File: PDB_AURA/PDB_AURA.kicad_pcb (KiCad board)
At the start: 4 copper layers, 50 x 50 mm, 55 parts, among them J100 XT30PW-M, J200 532617010, J201 XT30PW-F, J202 XT30PW-F, J203 XT30PW-F, J204 XT30PW-F, Q200 HSK10N06, Q201 HSK10N06, U101 SI4825DDY-T1-GE3, U2 TPS56C230RJER, U200 LTV-217-B-G, U201 LTV-217-B-G, U202 INA219AIDCNR

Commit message: Initial draft
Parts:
- TP102, TP105: moved to B.Cu
- moved TP105 46.7 mm to (68.0, 73.5), turned to 180 degrees
- moved TP101 36.6 mm to (75.0, 73.0)
- moved TP102 34.1 mm to (77.5, 76.0), turned to 180 degrees
- moved TP104 31.3 mm to (86.5, 80.5)
- moved TP103 30.6 mm to (81.0, 73.0)
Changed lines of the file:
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@@
 	(footprint "TestPoint:TestPoint_Pad_D1.0mm"
 		(layer "F.Cu")
-		(at 114.5 66.45)
+		(at 86.5 80.5)
 		(descr "SMD pad as test Point, diameter 1.0mm")
 		(tags "test point SMD pad")
@@
 	(footprint "TestPoint:TestPoint_Pad_D1.0mm"
 		(layer "F.Cu")
-		(at 111.45 69.5)
+		(at 75 73)
 		(descr "SMD pad as test Point, diameter 1.0mm")
 		(tags "test point SMD pad")
@@
 		)
 	)
-	(footprint "TestPoint:TestPoint_Pad_D1.0mm"
-		(layer "F.Cu")
-		(at 111.45 72.55)
-		(descr "SMD pad as test Point, diameter 1.0mm")
-		(tags "test point SMD pad")
-		(property "Reference" "TP102"
-			(at 0 -1.448 0)
-			(layer "F.SilkS")
-			(hide yes)
-			(effects
-				(font
-					(size 1 1)
-					(thickness 0.15)
-				)
-			)
-		)
-		(property "Value" "TestPoint"
-			(at 0 1.55 0)
-			(layer "F.Fab")
-			(effects
-				(font
-					(size 1 1)
-					(thickness 0.15)
-				)
-			)
-		)
-		(property "Datasheet" ""
-			(at 0 0 0)
-			(unlocked yes)
-			(layer "F.Fab")
-			(hide yes)
-			(effects
-				(font
-					(size 1.27 1.27)
-					(thickness 0.15)
-				)
-			)
-		)
-		(property "Description" "test point"
-			(at 0 0 0)
-			(unlocked yes)
-			(layer "F.Fab")
-			(hide yes)
-			(effects
-				(font
-					(size 1.27 1.27)
-					(thickness 0.15)
-				)
-			)
-		)
-		(property ki_fp_filters "Pin* Test*")
-		(sheetname "/100_Power/")
-		(sheetfile "Power.kicad_sch")
-		(attr exclude_from_pos_files)
-		(fp_circle
-			(center 0 0)
-			(end 0 0.7)
-			(stroke
-				(width 0.12)
-				(type solid)
-			)
-			(fill no)
-			(layer "F.SilkS")
-		)
-		(fp_circle
-			(center 0 0)
-			(end 1 0)
-			(stroke
-				(width 0.05)
-				(type solid)
-			)
-			(fill no)
-			(layer "F.CrtYd")
-		)
-		(fp_text user "${REFERENCE}"
-			(at 0 -1.45 0)
-			(layer "F.Fab")
-			(effects
-				(font
-					(size 1 1)
-					(thickness 0.15)
-				)
-			)
-		)
-		(pad "1" smd circle
-			(at 0 0)
-			(size 1 1)
-			(layers "F.Cu" "F.Mask")
-			(net 49 "/100_Power/FB_5V")
-			(pinfunction "1")
-			(pintype "passive")
-		)
-		(embedded_fonts no)
-	)
 	(footprint "Resistor_SMD:R_0402_1005Metric"
 		(layer "F.Cu")
@@
 	(footprint "TestPoint:TestPoint_Pad_D1.0mm"
 		(layer "F.Cu")
-		(at 111.45 75.6)
+		(at 81 73)
 		(descr "SMD pad as test Point, diameter 1.0mm")
 		(tags "test point SMD pad")
@@
 		(embedded_fonts no)
 	)
-	(footprint "TestPoint:TestPoint_Pad_D1.0mm"
-		(layer "F.Cu")
-		(at 114.5 69.5)
-		(descr "SMD pad as test Point, diameter 1.0mm")
-		(tags "test point SMD pad")
-		(property "Reference" "TP105"
-			(at 0 -1.448 0)
-			(layer "F.SilkS")
-			(hide yes)
-			(effects
-				(font
-					(size 1 1)
-					(thickness 0.15)
-				)
-			)
-		)
-		(property "Value" "TestPoint"
-			(at 0 1.55 0)
-			(layer "F.Fab")
-			(effects
-				(font
-					(size 1 1)
-					(thickness 0.15)
-				)
-			)
-		)
-		(property "Datasheet" ""
-			(at 0 0 0)
-			(unlocked yes)
-			(layer "F.Fab")
-			(hide yes)
-			(effects
-				(font
-					(size 1.27 1.27)
-					(thickness 0.15)
-				)
-			)
-		)
-		(property "Description" "test point"
-			(at 0 0 0)
-			(unlocked yes)
-			(layer "F.Fab")
-			(hide yes)
-			(effects
-				(font
-					(size 1.27 1.27)
-					(thickness 0.15)
-				)
-			)
-		)
-		(property ki_fp_filters "Pin* Test*")
-		(sheetname "/100_Power/")
-		(sheetfile "Power.kicad_sch")
-		(attr exclude_from_pos_files)
-		(fp_circle
-			(center 0 0)
-			(end 0 0.7)
-			(stroke
-				(width 0.12)
-				(type solid)
-			)
-			(fill no)
-			(layer "F.SilkS")
-		)
-		(fp_circle
-			(center 0 0)
-			(end 1 0)
-			(stroke
-				(width 0.05)
-				(type solid)
-			)
-			(fill no)
-			(layer "F.CrtYd")
-		)
-		(fp_text user "${REFERENCE}"
-			(at 0 -1.45 0)
-			(layer "F.Fab")
-			(effects
-				(font
-					(size 1 1)
-					(thickness 0.15)
-				)
-			)
-		)
-		(pad "1" smd circle
-			(at 0 0)
-			(size 1 1)
-			(layers "F.Cu" "F.Mask")
-			(net 7 "/100_Power/rvrs_plr")
-			(pinfunction "1")
-			(pintype "passive")
-		)
-		(embedded_fonts no)
-	)
 	(footprint "Resistor_SMD:R_0402_1005Metric"
 		(layer "F.Cu")
@@
 		)
 	)
+	(footprint "TestPoint:TestPoint_Pad_D1.0mm"
+		(layer "B.Cu")
+		(at 77.5 76 180)
+		(descr "SMD pad as test Point, diameter 1.0mm")
+		(tags "test point SMD pad")
+		(property "Reference" "TP102"
+			(at 0 1.448 0)
+			(layer "B.SilkS")
+			(hide yes)
+			(effects
+				(font
+					(size 1 1)
+					(thickness 0.15)
+				)
+				(justify mirror)
+			)
+		)
+		(property "Value" "TestPoint"
+			(at 0 -1.55 0)
+			(layer "B.Fab")
+			(effects
+				(font
+					(size 1 1)
+					(thickness 0.15)
+				)
+				(justify mirror)
+			)
+		)
+		(property "Datasheet" ""
+			(at 0 0 0)
+			(unlocked yes)
+			(layer "B.Fab")
+			(hide yes)
+			(effects
+				(font
+					(size 1.27 1.27)
+					(thickness 0.15)
+				)
+				(justify mirror)
+			)
+		)
+		(property "Description" "test point"
+			(at 0 0 0)
+			(unlocked yes)
+			(layer "B.Fab")
+			(hide yes)
+			(effects
+				(font
+					(size 1.27 1.27)
+					(thickness 0.15)
+				)
+				(justify mirror)
+			)
+		)
+		(property ki_fp_filters "Pin* Test*")
+		(sheetname "/100_Power/")
+		(sheetfile "Power.kicad_sch")
+		(attr exclude_from_pos_files)
+		(fp_circle
+			(center 0 0)
+			(end 0 -0.7)
+			(stroke
+				(width 0.12)
+				(type solid)
+			)
+			(fill no)
+			(layer "B.SilkS")
+		)
+		(fp_circle
+			(center 0 0)
+			(end 1 0)
+			(stroke
+				(width 0.05)
+				(type solid)
+			)
+			(fill no)
+			(layer "B.CrtYd")
+		)
+		(fp_text user "${REFERENCE}"
+			(at 0 1.45 0)
+			(layer "B.Fab")
+			(effects
+				(font
+					(size 1 1)
+					(thickness 0.15)
+				)
+				(justify mirror)
+			)
+		)
+		(pad "1" smd circle
+			(at 0 0 180)
+			(size 1 1)
+			(layers "B.Cu" "B.Mask")
+			(net 49 "/100_Power/FB_5V")
+			(pinfunction "1")
+			(pintype "passive")
+		)
+		(embedded_fonts no)
+	)
+	(footprint "TestPoint:TestPoint_Pad_D1.0mm"
+		(layer "B.Cu")
+		(at 68 73.5 180)
+		(descr "SMD pad as test Point, diameter 1.0mm")
+		(tags "test point SMD pad")
+		(property "Reference" "TP105"
+			(at 0 1.448 0)
+			(layer "B.SilkS")
+			(hide yes)
+			(effects
+				(font
+					(size 1 1)
+					(thickness 0.15)
+				)
+				(justify mirror)
+			)
+		)
+		(property "Value" "TestPoint"
+			(at 0 -1.55 0)
+			(layer "B.Fab")
+			(effects
+				(font
+					(size 1 1)
+					(thickness 0.15)
+				)
+				(justify mirror)
+			)
+		)
+		(property "Datasheet" ""
+			(at 0 0 0)
+			(unlocked yes)
+			(layer "B.Fab")
+			(hide yes)
+			(effects
+				(font
+					(size 1.27 1.27)
+					(thickness 0.15)
+				)
+				(justify mirror)
+			)
+		)
+		(property "Description" "test point"
+			(at 0 0 0)
+			(unlocked yes)
+			(layer "B.Fab")
+			(hide yes)
+			(effects
+				(font
+					(size 1.27 1.27)
+					(thickness 0.15)
+				)
+				(justify mirror)
+			)
+		)
+		(property ki_fp_filters "Pin* Test*")
+		(sheetname "/100_Power/")
+		(sheetfile "Power.kicad_sch")
+		(attr exclude_from_pos_files)
+		(fp_circle
+			(center 0 0)
+			(end 0 -0.7)
+			(stroke
+				(width 0.12)
+				(type solid)
+			)
+			(fill no)
+			(layer "B.SilkS")
+		)
+		(fp_circle
+			(center 0 0)
+			(end 1 0)
+			(stroke
+				(width 0.05)
+				(type solid)
+			)
+			(fill no)
+			(layer "B.CrtYd")
+		)
+		(fp_text user "${REFERENCE}"
+			(at 0 1.45 0)
+			(layer "B.Fab")
+			(effects
+				(font
+					(size 1 1)
+					(thickness 0.15)
+				)
+				(justify mirror)
+			)
+		)
+		(pad "1" smd circle
+			(at 0 0 180)
+			(size 1 1)
+			(layers "B.Cu" "B.Mask")
+			(net 7 "/100_Power/rvrs_plr")
+			(pinfunction "1")
+			(pintype "passive")
+		)
+		(embedded_fonts no)
+	)
 	(gr_arc

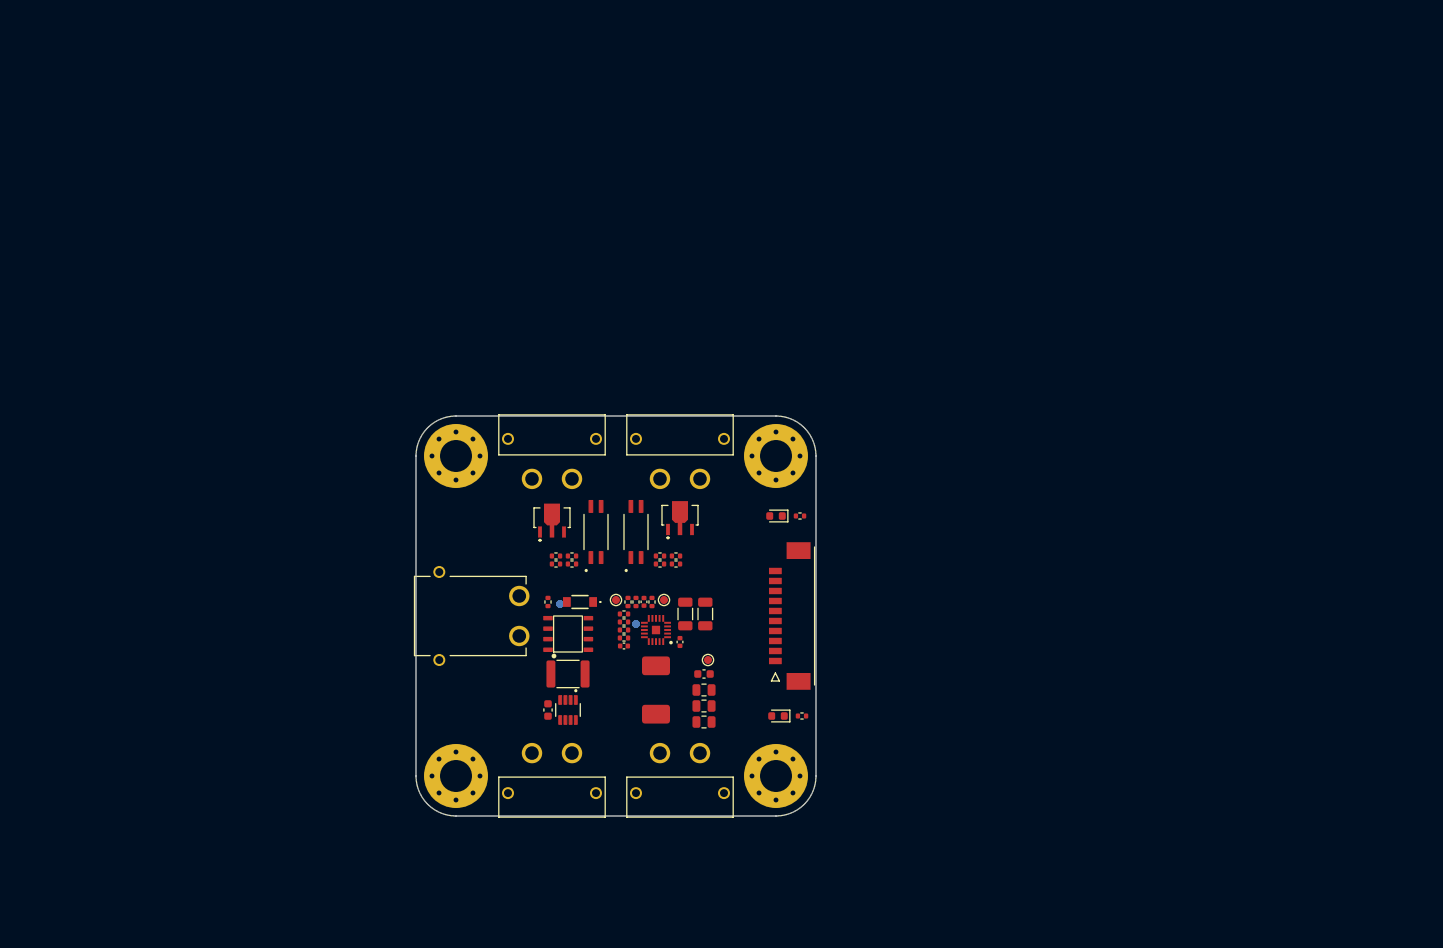
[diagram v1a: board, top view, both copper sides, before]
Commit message: New PDB specs chosen
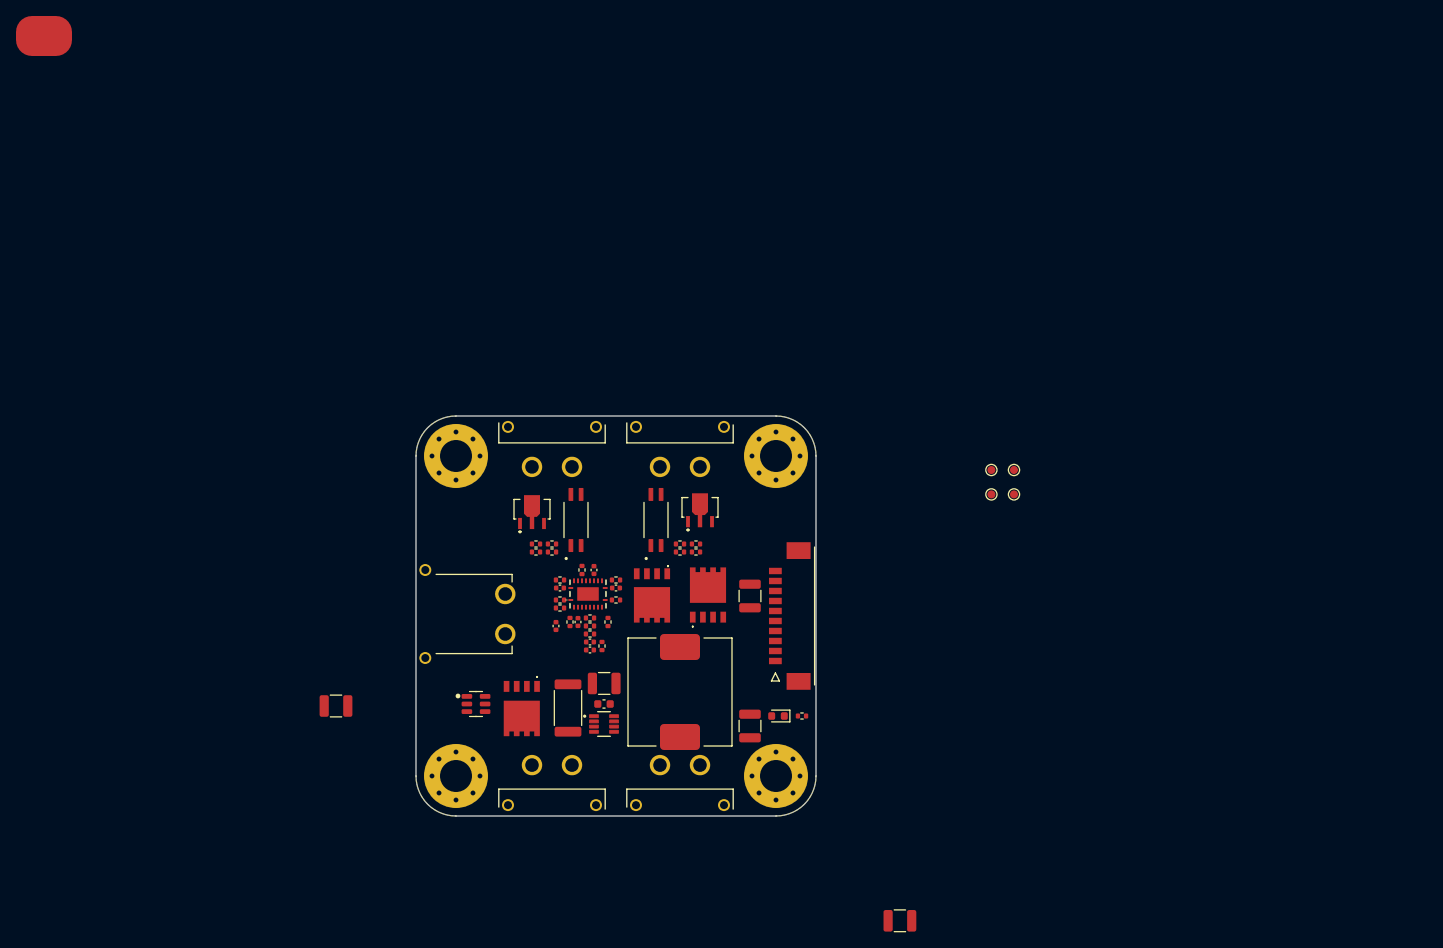
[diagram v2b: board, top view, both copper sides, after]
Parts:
- removed C100: 1u, Capacitor_SMD:C_0402_1005Metric
- removed C101, C102: 22u, Capacitor_SMD:C_1206_3216Metric
- removed C103: 18n, Capacitor_SMD:C_0402_1005Metric
- removed C104: 100n, Capacitor_SMD:C_0402_1005Metric
- removed C105: 100n, Capacitor_SMD:C_0603_1608Metric
- removed C106, C107, C108: 22u, Capacitor_SMD:C_0805_2012Metric
- removed D1: MMSZ5242B, MMSZ5252B:MMSZ5252B
- removed D100: LED, LED_SMD:LED_0603_1608Metric
- removed L100: 1u8, CKST0603:CKST0603-1.5uHM
- removed R102: 49k, Resistor_SMD:R_0402_1005Metric
- removed R103: 13k, Resistor_SMD:R_0402_1005Metric
- removed R104: 180k, Resistor_SMD:R_0402_1005Metric
- removed R105: 33k, Resistor_SMD:R_0402_1005Metric
- removed R106: 330k, Resistor_SMD:R_0402_1005Metric
- removed R107: 110k, Resistor_SMD:R_0402_1005Metric
- removed R108: 15k, Resistor_SMD:R_0402_1005Metric
- removed R109: 680R, Resistor_SMD:R_0402_1005Metric
- removed R110: 100k, Resistor_SMD:R_0402_1005Metric
- removed R111: 0m5, Resistor_SMD:R_1812_4532Metric
- removed TP101, TP102, TP103, TP104, TP105: TestPoint, TestPoint:TestPoint_Pad_D1.0mm
- removed U101: SI4825DDY-T1-GE3, SI4825DDY-T1-GE3:SI4825DDY-T1-GE3
- added C1: 1n, Capacitor_SMD:C_0402_1005Metric, F.Cu at (71.8, 79.2)
- added C10: 47u, Capacitor_SMD:C_1210_3225Metric, F.Cu at (91.8, 72.5)
- added C11: 47u, Capacitor_SMD:C_1210_3225Metric, F.Cu at (73.5, 83.4)
- added C12: 22u, Capacitor_SMD:C_1210_3225Metric, F.Cu at (40.0, 86.2)
- added C13: 22u, Capacitor_SMD:C_1210_3225Metric, F.Cu at (110.5, 113.1)
- added C2: 8n2, Capacitor_SMD:C_0402_1005Metric, F.Cu at (67.5, 76.2)
- added C3: 100n, Capacitor_SMD:C_0402_1005Metric, F.Cu at (70.2, 75.8)
- added C4: 390p, Capacitor_SMD:C_0402_1005Metric, F.Cu at (71.8, 78.2)
- added C5: 100n, Resistor_SMD:R_0402_1005Metric, F.Cu at (70.8, 69.2)
- added C6: 2u2, Capacitor_SMD:C_0402_1005Metric, F.Cu at (72.2, 69.2)
- added C7: 10p, Capacitor_SMD:C_0402_1005Metric, F.Cu at (75.0, 71.5)
- added C8: 100n, Capacitor_SMD:C_0402_1005Metric, F.Cu at (68.0, 71.5)
- added C9: 47u, Capacitor_SMD:C_1210_3225Metric, F.Cu at (91.8, 88.8)
- added J1: ~, SOLDER_PAD:PWR_SOLDER_PAD, F.Cu at (3.50, 2.50)
- added L1: 1u8, 125CDMCCDS-1R8MC:Untitled, F.Cu at (83.0, 84.5)
- added Q1: CSD18540Q5B, CSD18540Q5B:CSD18540Q5B, F.Cu at (86.5, 72.4)
- added Q2: CSD18510Q5B, CSD18510Q5B:CSD18540Q5BT, F.Cu at (79.5, 72.6)
- added Q3: CSD18540Q5B, CSD18540Q5B:CSD18540Q5B, F.Cu at (63.2, 86.6)
- added R1: 18k, Resistor_SMD:R_0402_1005Metric, F.Cu at (71.8, 76.2)
- added R10: 9k1, Resistor_SMD:R_0402_1005Metric, F.Cu at (68.0, 74.0)
- added R11: 2R1, Resistor_SMD:R_0402_1005Metric, F.Cu at (68.0, 70.5)
- added R12: 0m5, Resistor_SMD:R_2512_6332Metric, F.Cu at (69.0, 86.5)
- added R2: 3k4, Resistor_SMD:R_0402_1005Metric, F.Cu at (71.8, 75.2)
- added R3: 1k47, Resistor_SMD:R_0402_1005Metric, F.Cu at (71.8, 77.2)
- added R4: 4k7, Resistor_SMD:R_0402_1005Metric, F.Cu at (69.2, 75.8)
- added R5: 249R, Resistor_SMD:R_0402_1005Metric, F.Cu at (73.2, 78.8)
- added R6: 20k, Resistor_SMD:R_0402_1005Metric, F.Cu at (74.0, 75.8)
- added R7: 576R, Resistor_SMD:R_0402_1005Metric, F.Cu at (75.0, 70.5)
- added R8: 4k7, Resistor_SMD:R_0402_1005Metric, F.Cu at (75.0, 73.0)
- added R9: 35k7, Resistor_SMD:R_0402_1005Metric, F.Cu at (68.0, 73.0)
- added TP1: TestPoint, TestPoint:TestPoint_Pad_D1.0mm, F.Cu at (124.8, 56.8)
- added TP2: TestPoint, TestPoint:TestPoint_Pad_D1.0mm, F.Cu at (124.8, 59.8)
- added TP3: TestPoint, TestPoint:TestPoint_Pad_D1.0mm, F.Cu at (121.9, 56.8)
- added TP4: TestPoint, TestPoint:TestPoint_Pad_D1.0mm, F.Cu at (121.9, 59.8)
- added U1: LM25145RGYR, LM24145RGYR:RGY0020B, F.Cu at (71.5, 72.2)
- U2: value TPS56C230RJER -> LM74700; footprint TPS56C230RJER:QFN45P300X300X100-21N-D -> Package_TO_SOT_SMD:SOT-23-6
- moved U2 24.3 mm to (57.5, 86.0), turned to 0 degrees
- moved C200 7.04 mm to (73.5, 86.0), turned to 180 degrees
- moved U202 4.83 mm to (73.5, 88.5), turned to 0 degrees
- moved R200 2.92 mm to (65.0, 67.0)
- moved R201 2.92 mm to (67.0, 67.0)
- moved R202 2.92 mm to (65.0, 66.0)
- moved R203 2.92 mm to (67.0, 66.0)
- moved R204 2.92 mm to (85.0, 67.0)
- moved R205 2.92 mm to (83.0, 67.0)
- moved R206 2.92 mm to (85.0, 66.0)
- moved R207 2.92 mm to (83.0, 66.0)
- moved U200 2.92 mm to (70.0, 63.0)
- moved U201 2.92 mm to (80.0, 63.0)
- moved Q200 2.72 mm to (64.5, 62.9)
- moved Q201 2.69 mm to (85.5, 62.6)
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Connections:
- U2 pad 1: /100_Power/BST_5V -> /100_Power/VCAP
- U2 pad 2: +BATT_FILT -> GND
- U2 pad 3: +BATT_FILT -> +BATT
- U2 pad 4: +BATT_FILT -> INA_IN+
- U2 pad 5: +BATT_FILT -> /100_Power/PLR_G
- U2 pad 6: /100_Power/SW_5V -> +BATT

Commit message: Moving to laptop
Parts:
- removed C13: 22u, Capacitor_SMD:C_1210_3225Metric
- added C14: 22u, Capacitor_SMD:C_1210_3225Metric, F.Cu at (94.5, 87.8)
- added C15: 22u, Capacitor_SMD:C_1210_3225Metric, B.Cu at (94.5, 87.8)
- added C16: 22u, Capacitor_SMD:C_1210_3225Metric, F.Cu at (76.2, 82.5)
- added C4: 390p, Capacitor_SMD:C_0402_1005Metric, F.Cu at (62.0, 86.8)
- added D1: LED, LED_SMD:LED_0603_1608Metric, F.Cu at (95.5, 61.5)
- added J10: ~, SOLDER_PAD:BAT_SOLDER_PAD, F.Cu at (55.2, 63.8)
- added J2: ~, SOLDER_PAD:PWR_SOLDER_PAD, B.Cu at (85.5, 53.5)
- added J3: ~, SOLDER_PAD:PWR_SOLDER_PAD, B.Cu at (64.5, 53.5)
- added J4: ~, SOLDER_PAD:PWR_SOLDER_PAD, B.Cu at (69.5, 53.5)
- added J5: ~, SOLDER_PAD:PWR_SOLDER_PAD, B.Cu at (85.5, 96.5)
- added J6: ~, SOLDER_PAD:PWR_SOLDER_PAD, B.Cu at (64.5, 96.5)
- added J7: ~, SOLDER_PAD:PWR_SOLDER_PAD, B.Cu at (80.5, 53.5)
- added J8: ~, SOLDER_PAD:PWR_SOLDER_PAD, B.Cu at (80.5, 96.5)
- added J9: ~, SOLDER_PAD:BAT_SOLDER_PAD, F.Cu at (55.2, 86.2)
- added R13: 4k7, Resistor_SMD:R_0402_1005Metric, F.Cu at (98.5, 61.5)
- C11, C9: value 47u -> 22u
- J1, TP1, TP3, TP4: moved to B.Cu
- moved J1 114.9 mm to (69.5, 96.5), turned to 180 degrees
- moved TP2 57.5 mm to (68.0, 68.8)
- moved TP1 55.8 mm to (71.8, 74.2), turned to 180 degrees
- moved TP3 51.3 mm to (73.8, 74.2), turned to 180 degrees
- moved TP4 45.9 mm to (89.0, 91.8), turned to 180 degrees
- moved D101 24.3 mm to (95.5, 63.2)
- moved R112 24.3 mm to (98.5, 63.2)
- moved C12 23.1 mm to (62.8, 82.5), turned to 180 degrees
- moved C10 21.1 mm to (76.2, 86.8), turned to 0 degrees
- moved C2 9.82 mm to (70.0, 66.8), turned to 0 degrees
- moved C1 9.52 mm to (67.0, 71.0), turned to 90 degrees
- moved R5 8.49 mm to (67.5, 72.5), turned to 180 degrees
- moved Q3 8.42 mm to (69.3, 80.8), turned to 0 degrees
- moved R11 8.40 mm to (75.8, 67.2), turned to 90 degrees
- moved C4 8.16 mm to (68.0, 71.0), turned to 90 degrees
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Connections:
- C11 pad 1: +BATT_FILT -> INA_IN+
- J1 pad 1: unconnected-(J1-Pad1) -> +BATT_FILT
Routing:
- net GND: vias 0 -> 182
- net +BATT_FILT: vias 0 -> 140
- net +BATT: vias 0 -> 42
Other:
- board text added: "J1"
